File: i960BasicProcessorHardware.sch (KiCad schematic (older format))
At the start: 66 parts, among them J1 Conn_01x08, J10 Conn_02x39_Odd_Even, J2 Conn_02x05_Odd_Even, J3 Conn_02x05_Odd_Even, J4 Conn_02x05_Odd_Even, J5 Conn_02x16_Odd_Even, J6 Conn_01x03, J7 Conn_01x03, J8 Conn_01x06, J9 Conn_01x11, U1 74HC245, U10 Adafruit_FeatherWing (PSRAM F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, U11 Adafruit_FeatherWing (PSRAM F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, U12 74LS125, U13 74LS04, U14 74LS08, U15 74LS174, U16 SN74LVC245AN, U17 74LS174, U2 80960Sx, U3 MCP23S17_SP, U4 MCP23S17_SP, U5 74HC245, U6 74HC573, U7 74HC573, U8 MCP23S17_SP, U9 MCP23S17_SP

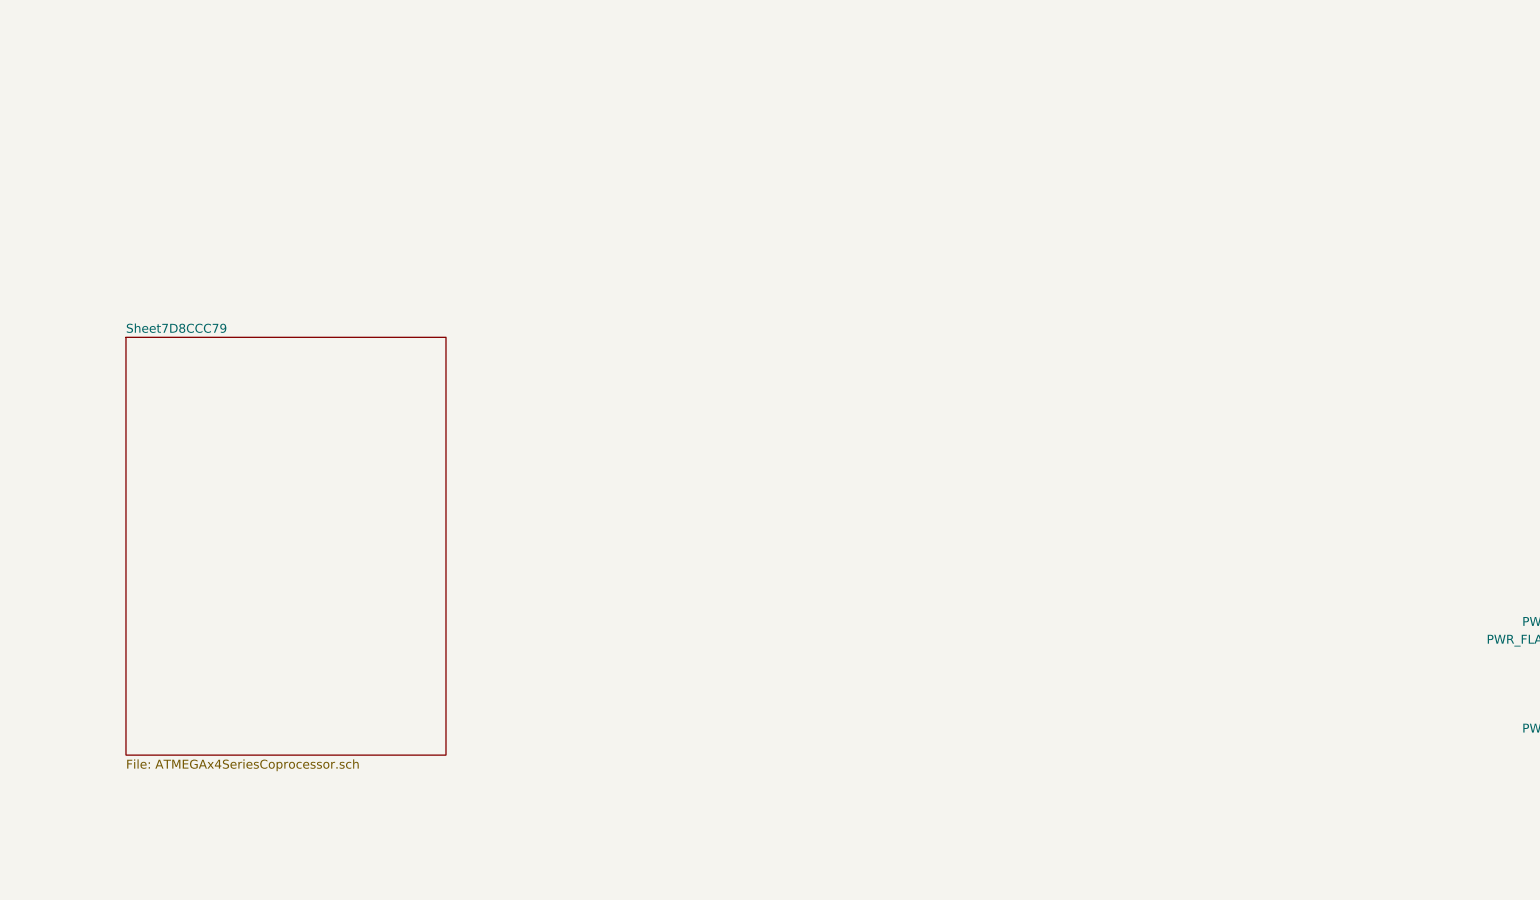
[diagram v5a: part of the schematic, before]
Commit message: Partially pinout the extra x4 hardware
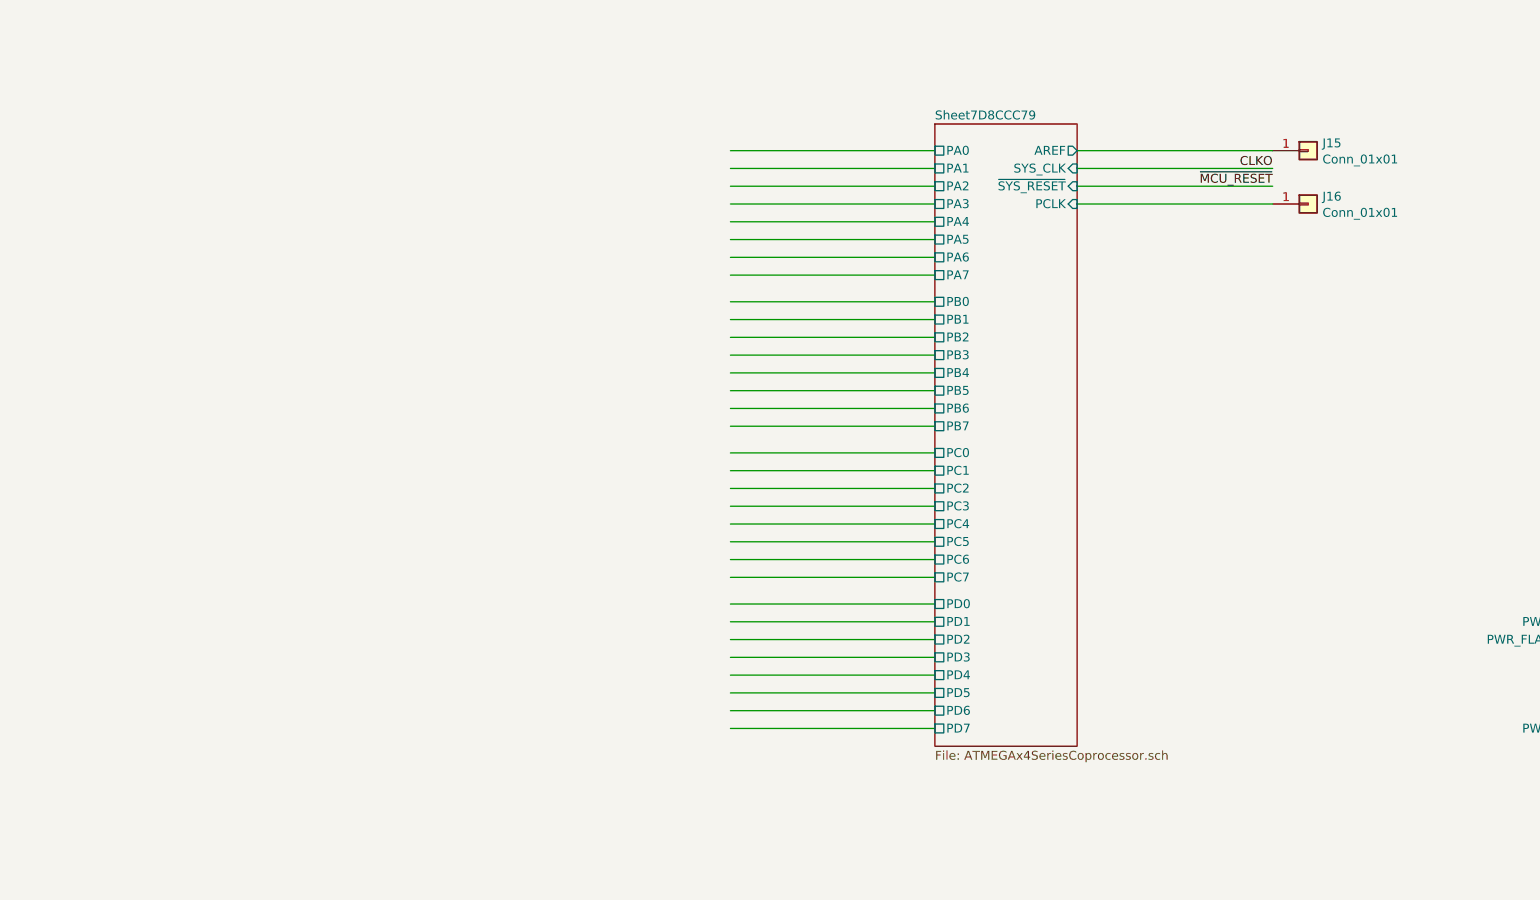
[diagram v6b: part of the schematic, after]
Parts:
- added J15, J16: Conn_01x01, Connector_PinHeader_2.54mm:PinHeader_1x01_P2.54mm_Vertical, symbol Connector_Generic:Conn_01x01
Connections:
- wire segments 734 -> 770
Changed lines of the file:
@@
 NoConn ~ 27900 21350
 $Sheet
-S 20200 2300 1800 2350
+S 24750 1100 800  3500
 U 7D8CCC7A
 F0 "Sheet7D8CCC79" 50
 F1 "ATMEGAx4SeriesCoprocessor.sch" 50
+F2 "SYS_CLK" I R 25550 1350 50
+F3 "AREF" O R 25550 1250 50
+F4 "PA0" U L 24750 1250 50
+F5 "PA1" U L 24750 1350 50
+F6 "PA2" U L 24750 1450 50
+F7 "PA3" U L 24750 1550 50
+F8 "PA4" U L 24750 1650 50
+F9 "PA5" U L 24750 1750 50
+F10 "PA6" U L 24750 1850 50
+F11 "PA7" U L 24750 1950 50
+F12 "PB0" U L 24750 2100 50
+F13 "PB1" U L 24750 2200 50
+F14 "PB2" U L 24750 2300 50
+F15 "PB3" U L 24750 2400 50
+F16 "PB4" U L 24750 2500 50
+F17 "PC0" U L 24750 2950 50
+F18 "PC1" U L 24750 3050 50
+F19 "PC2" U L 24750 3150 50
+F20 "PC3" U L 24750 3250 50
+F21 "PC4" U L 24750 3350 50
+F22 "PC5" U L 24750 3450 50
+F23 "PC6" U L 24750 3550 50
+F24 "PC7" U L 24750 3650 50
+F25 "PD2" U L 24750 4000 50
+F26 "PD3" U L 24750 4100 50
+F27 "PD4" U L 24750 4200 50
+F28 "PD5" U L 24750 4300 50
+F29 "PD6" U L 24750 4400 50
+F30 "PB5" U L 24750 2600 50
+F31 "PB6" U L 24750 2700 50
+F32 "PB7" U L 24750 2800 50
+F33 "PD0" U L 24750 3800 50
+F34 "PD1" U L 24750 3900 50
+F35 "PD7" U L 24750 4500 50
+F36 "~SYS_RESET" I R 25550 1450 50
+F37 "PCLK" I R 25550 1550 50
 $EndSheet
+Wire Wire Line
+	25550 1250 26650 1250
+Wire Wire Line
+	25550 1350 26650 1350
+Wire Wire Line
+	25550 1450 26650 1450
+Wire Wire Line
+	25550 1550 26650 1550
+$Comp
+L Connector_Generic:Conn_01x01 J16
+U 1 1 7DEF5BF3
+P 26850 1550
+F 0 "J16" H 26930 1592 50  0000 L CNN
+F 1 "Conn_01x01" H 26930 1501 50  0000 L CNN
+F 2 "Connector_PinHeader_2.54mm:PinHeader_1x01_P2.54mm_Vertical" H 26850 1550 50  0001 C CNN
+F 3 "~" H 26850 1550 50  0001 C CNN
+	1    26850 1550
+	1    0    0    -1
+$EndComp
+Text Label 26650 1450 2    50   ~ 0
+~MCU_RESET
+Text Label 26650 1350 2    50   ~ 0
+CLKO
+$Comp
+L Connector_Generic:Conn_01x01 J15
+U 1 1 7DFB4B1C
+P 26850 1250
+F 0 "J15" H 26930 1292 50  0000 L CNN
+F 1 "Conn_01x01" H 26930 1201 50  0000 L CNN
+F 2 "Connector_PinHeader_2.54mm:PinHeader_1x01_P2.54mm_Vertical" H 26850 1250 50  0001 C CNN
+F 3 "~" H 26850 1250 50  0001 C CNN
+	1    26850 1250
+	1    0    0    -1
+$EndComp
+Wire Wire Line
+	24750 1250 23600 1250
+Wire Wire Line
+	24750 1350 23600 1350
+Wire Wire Line
+	24750 1450 23600 1450
+Wire Wire Line
+	24750 1550 23600 1550
+Wire Wire Line
+	24750 1650 23600 1650
+Wire Wire Line
+	24750 1750 23600 1750
+Wire Wire Line
+	24750 1850 23600 1850
+Wire Wire Line
+	24750 1950 23600 1950
+Wire Wire Line
+	24750 2100 23600 2100
+Wire Wire Line
+	24750 2200 23600 2200
+Wire Wire Line
+	24750 2300 23600 2300
+Wire Wire Line
+	24750 2400 23600 2400
+Wire Wire Line
+	24750 2500 23600 2500
+Wire Wire Line
+	24750 2600 23600 2600
+Wire Wire Line
+	24750 2700 23600 2700
+Wire Wire Line
+	24750 2800 23600 2800
+Wire Wire Line
+	24750 2950 23600 2950
+Wire Wire Line
+	24750 3050 23600 3050
+Wire Wire Line
+	24750 3150 23600 3150
+Wire Wire Line
+	24750 3250 23600 3250
+Wire Wire Line
+	24750 3350 23600 3350
+Wire Wire Line
+	24750 3450 23600 3450
+Wire Wire Line
+	24750 3550 23600 3550
+Wire Wire Line
+	24750 3650 23600 3650
+Wire Wire Line
+	24750 3800 23600 3800
+Wire Wire Line
+	24750 3900 23600 3900
+Wire Wire Line
+	24750 4000 23600 4000
+Wire Wire Line
+	24750 4100 23600 4100
+Wire Wire Line
+	24750 4200 23600 4200
+Wire Wire Line
+	24750 4300 23600 4300
+Wire Wire Line
+	24750 4400 23600 4400
+Wire Wire Line
+	24750 4500 23600 4500
 $EndSCHEMATC

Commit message: start moving the 74lvc245 to free up some space
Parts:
- U16: footprint digikey-footprints:DIP-20_W7.62mm -> Package_DIP:DIP-20_W7.62mm_Socket
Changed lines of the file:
@@
 F 0 "U16" H 25300 13203 60  0000 C CNN
 F 1 "SN74LVC245AN" H 25300 13097 60  0000 C CNN
-F 2 "digikey-footprints:DIP-20_W7.62mm" H 25600 12900 60  0001 L CNN
+F 2 "Package_DIP:DIP-20_W7.62mm_Socket" H 25600 12900 60  0001 L CNN
 F 3 "http://www.ti.com/general/docs/suppproductinfo.tsp?distId=10&gotoUrl=http%3A%2F%2Fwww.ti.com%2Flit%2Fgpn%2Fsn74lvc245a" H 25600 13000 60  0001 L CNN
 F 4 "296-8503-5-ND" H 25600 13100 60  0001 L CNN "Digi-Key_PN"

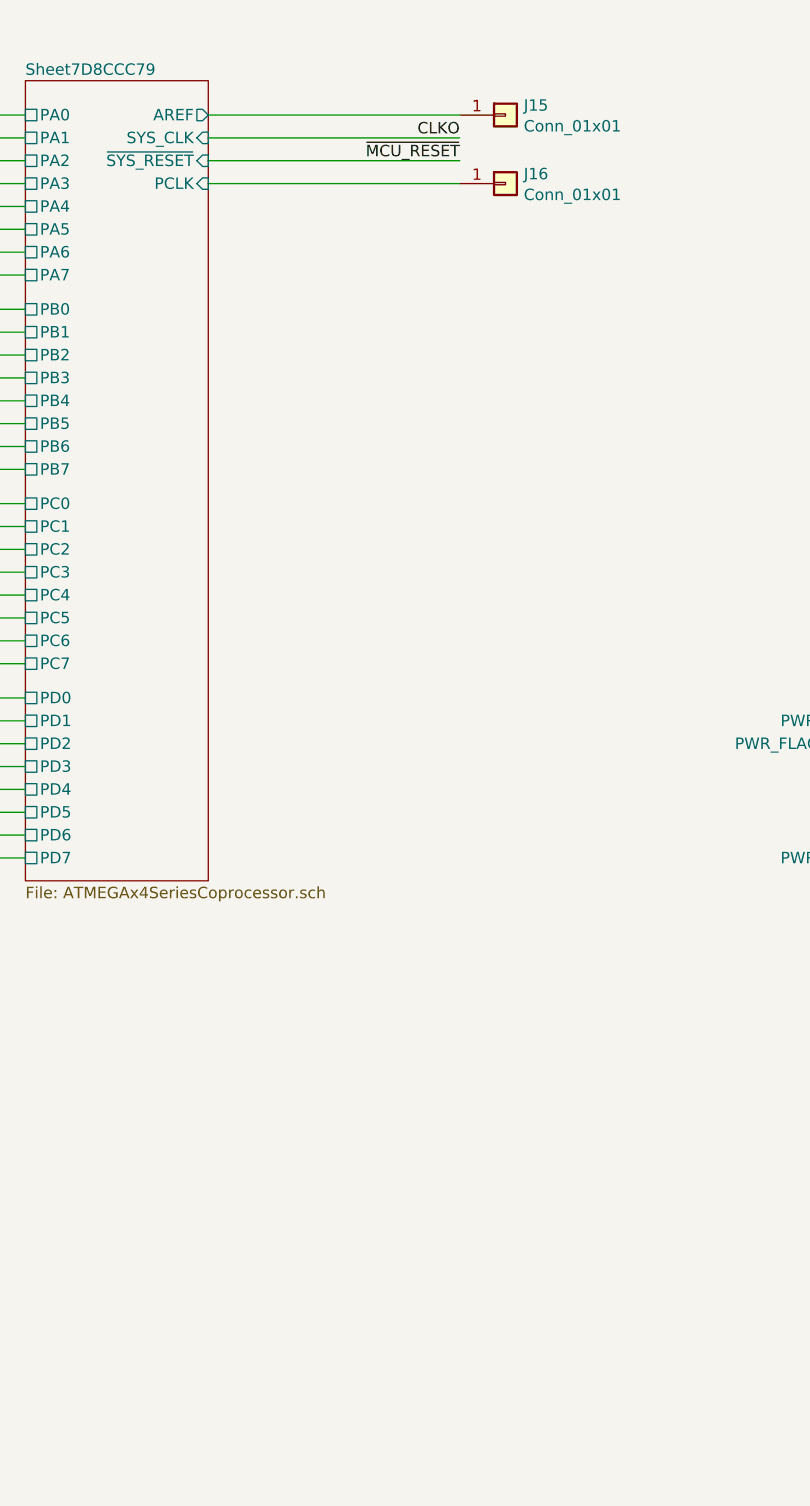
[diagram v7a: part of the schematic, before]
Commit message: Add an onboard oscillator when it is necessary to program the secondary processor
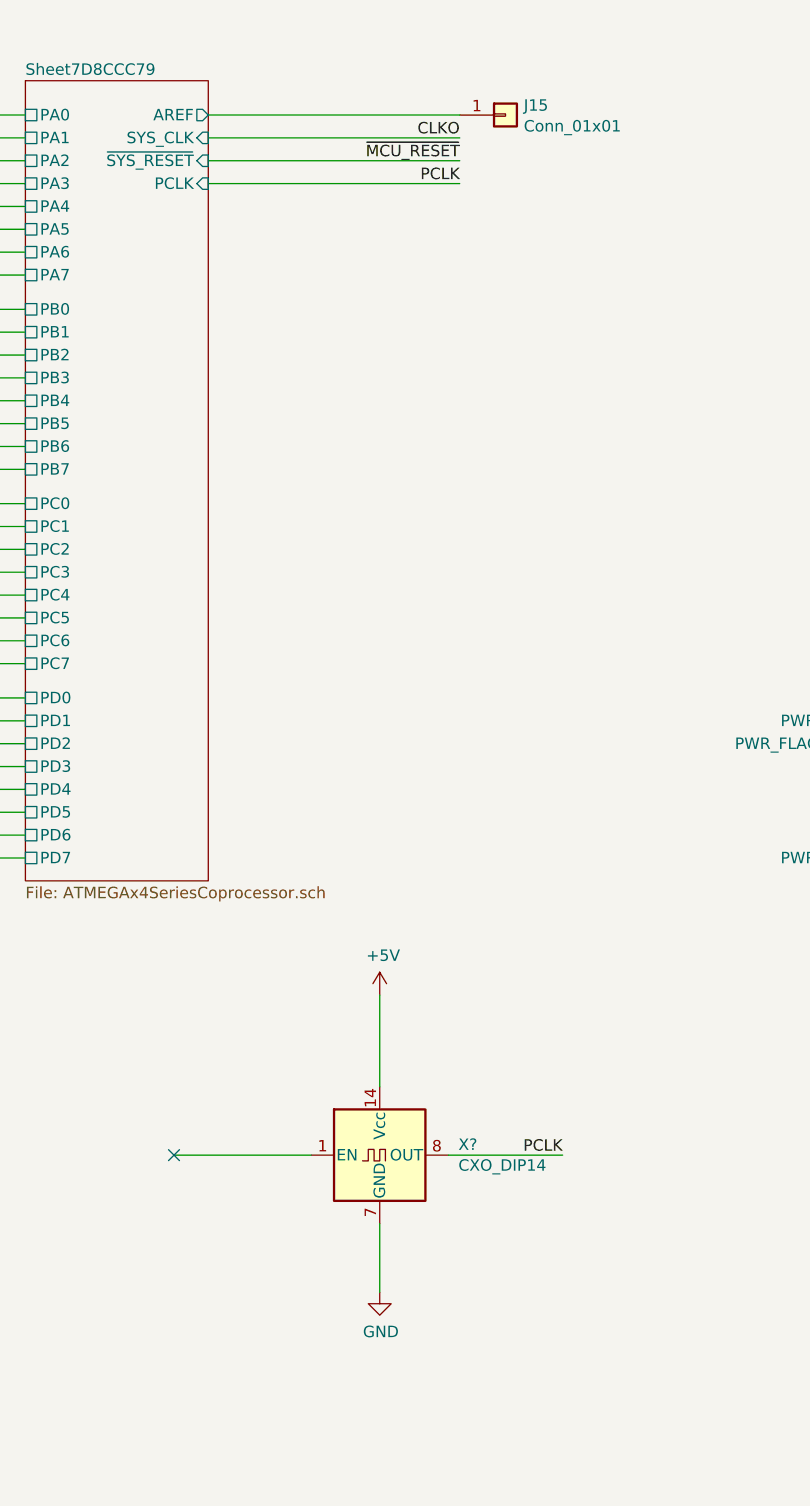
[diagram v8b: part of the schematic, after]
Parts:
- removed J16: Conn_01x01, Connector_PinHeader_2.54mm:PinHeader_1x01_P2.54mm_Vertical, symbol Connector_Generic:Conn_01x01
- added X?: CXO_DIP14, Oscillator:Oscillator_DIP-14, symbol Oscillator:CXO_DIP14
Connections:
- net labels added: PCLK
- wire segments 770 -> 774
- no-connect marks 86 -> 87
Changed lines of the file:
@@
 Wire Wire Line
 	25550 1550 26650 1550
-$Comp
-L Connector_Generic:Conn_01x01 J16
-U 1 1 7DEF5BF3
-P 26850 1550
-F 0 "J16" H 26930 1592 50  0000 L CNN
-F 1 "Conn_01x01" H 26930 1501 50  0000 L CNN
-F 2 "Connector_PinHeader_2.54mm:PinHeader_1x01_P2.54mm_Vertical" H 26850 1550 50  0001 C CNN
-F 3 "~" H 26850 1550 50  0001 C CNN
-	1    26850 1550
-	1    0    0    -1
-$EndComp
 Text Label 26650 1450 2    50   ~ 0
 ~MCU_RESET
@@
 Wire Wire Line
 	24750 4500 23600 4500
+$Comp
+L Oscillator:CXO_DIP14 X?
+U 1 1 7E8F4FC6
+P 26300 5800
+F 0 "X?" H 26644 5846 50  0000 L CNN
+F 1 "CXO_DIP14" H 26644 5755 50  0000 L CNN
+F 2 "Oscillator:Oscillator_DIP-14" H 26750 5450 50  0001 C CNN
+F 3 "http://cdn-reichelt.de/documents/datenblatt/B400/OSZI.pdf" H 26200 5800 50  0001 C CNN
+	1    26300 5800
+	1    0    0    -1
+$EndComp
+Wire Wire Line
+	26000 5800 25400 5800
+NoConn ~ 25400 5800
+Wire Wire Line
+	26300 5500 26300 5100
+Wire Wire Line
+	26300 6100 26300 6400
+Wire Wire Line
+	26600 5800 27100 5800
+Text Label 27100 5800 2    50   ~ 0
+PCLK
+$Comp
+L power:GND #PWR?
+U 1 1 7ECFA12B
+P 26300 6400
+F 0 "#PWR?" H 26300 6150 50  0001 C CNN
+F 1 "GND" H 26305 6227 50  0000 C CNN
+F 2 "" H 26300 6400 50  0001 C CNN
+F 3 "" H 26300 6400 50  0001 C CNN
+	1    26300 6400
+	1    0    0    -1
+$EndComp
+Text Label 26650 1550 2    50   ~ 0
+PCLK
+$Comp
+L power:+5V #PWR?
+U 1 1 7ECFB689
+P 26300 5100
+AR Path="/640CD6D6/7ECFB689" Ref="#PWR?"  Part="1"
+AR Path="/7ECFB689" Ref="#PWR?"  Part="1"
+F 0 "#PWR?" H 26300 4950 50  0001 C CNN
+F 1 "+5V" H 26315 5273 50  0000 C CNN
+F 2 "" H 26300 5100 50  0001 C CNN
+F 3 "" H 26300 5100 50  0001 C CNN
+	1    26300 5100
+	1    0    0    -1
+$EndComp
 $EndSCHEMATC
